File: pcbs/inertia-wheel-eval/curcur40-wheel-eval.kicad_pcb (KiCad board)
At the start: 2 copper layers, 48 x 32 mm, 13 parts, among them J1 SM06B-SRSS-TB, J2 AS5600_Wires, SW1 Kailh_Silent_6.2x6.2, U1 Waveshare_RP2040-Zero

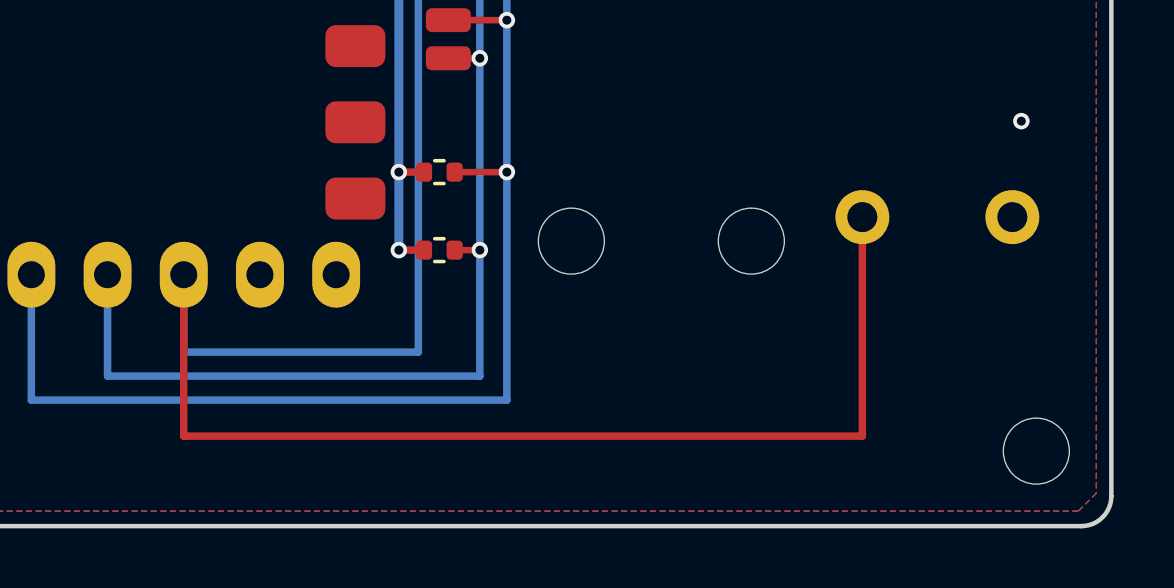
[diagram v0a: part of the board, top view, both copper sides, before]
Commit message: feat(pcb): trim wheel-sensor upper outline for pyramid cover and align eval SW1
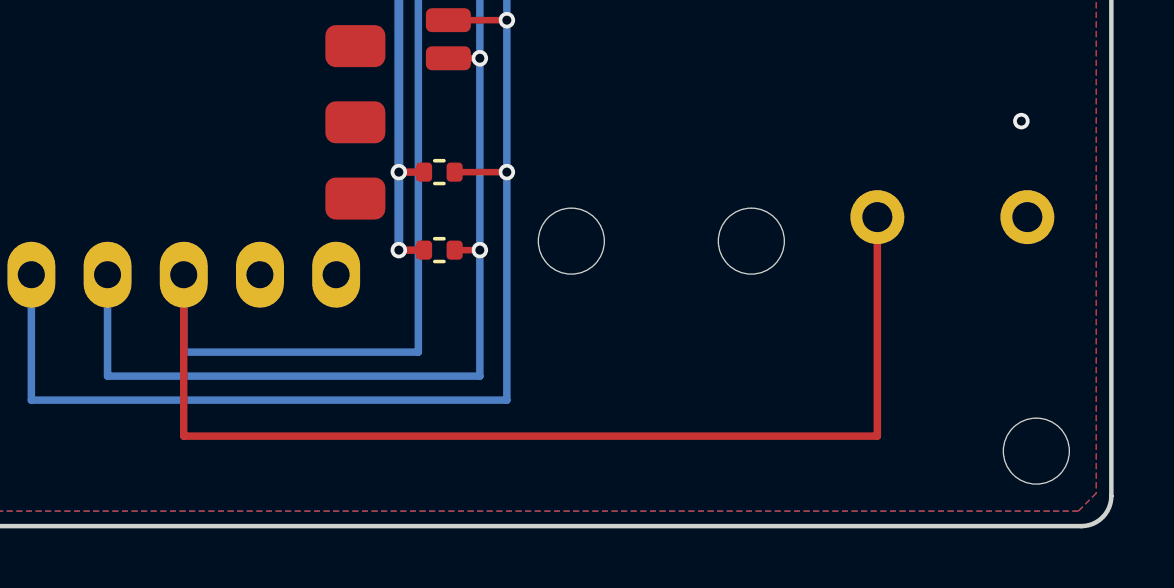
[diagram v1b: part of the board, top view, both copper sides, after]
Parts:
- moved SW1 0.50 mm to (118.7, 105.7)
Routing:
- net /SW_MID: track 68.1 -> 68.6 mm
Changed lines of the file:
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@@
 				(font
 					(size 1.27 1.27)
+					(thickness 0.15)
 				)
 			)
@@
 				(font
 					(size 1.27 1.27)
+					(thickness 0.15)
 				)
 			)
@@
 	(footprint "kbd:Kailh_Square_Silent_6.2x6.2mm"
 		(layer "F.Cu")
-		(at 118.2 105.7)
+		(at 118.7 105.7)
 		(descr "Kailh Square Silent Micro Switch 6.2x6.2x4.3mm (CMI624301D09)")
 		(property "Reference" "SW1"
@@
 				(font
 					(size 1.27 1.27)
+					(thickness 0.15)
 				)
 			)
@@
 				(font
 					(size 1.27 1.27)
+					(thickness 0.15)
 				)
 			)
@@
 	)
 	(segment
+		(start 103.85 99.135)
+		(end 101.9 99.135)
+		(width 0.22)
+		(layer "F.Cu")
+		(net "/SDA")
+	)
+	(segment
+		(start 103.85 104.2)
+		(end 102.11 104.2)
+		(width 0.22)
+		(layer "F.Cu")
+		(net "/SDA")
+	)
+	(segment
+		(start 104.5 92.2)
+		(end 104.5 89.4)
+		(width 0.22)
+		(layer "F.Cu")
+		(net "/SDA")
+	)
+	(via
+		(at 103.85 104.2)
+		(size 0.55)
+		(drill 0.3)
+		(layers "F.Cu" "B.Cu")
+		(net "/SDA")
+	)
+	(via
+		(at 103.85 99.135)
+		(size 0.55)
+		(drill 0.3)
+		(layers "F.Cu" "B.Cu")
+		(net "/SDA")
+	)
+	(via
+		(at 104.5 92.2)
+		(size 0.55)
+		(drill 0.3)
+		(layers "F.Cu" "B.Cu")
+		(net "/SDA")
+	)
+	(segment
+		(start 103.85 104.2)
+		(end 103.85 99.135)
+		(width 0.25)
+		(layer "B.Cu")
+		(net "/SDA")
+	)
+	(segment
+		(start 88 107.62)
+		(end 88 111.8)
+		(width 0.25)
+		(layer "B.Cu")
+		(net "/SDA")
+	)
+	(segment
+		(start 88 111.8)
+		(end 103.85 111.8)
+		(width 0.25)
+		(layer "B.Cu")
+		(net "/SDA")
+	)
+	(segment
+		(start 103.85 111.8)
+		(end 103.85 104.2)
+		(width 0.25)
+		(layer "B.Cu")
+		(net "/SDA")
+	)
+	(segment
+		(start 103.85 99.135)
+		(end 103.85 92.2)
+		(width 0.25)
+		(layer "B.Cu")
+		(net "/SDA")
+	)
+	(segment
+		(start 103.85 92.2)
+		(end 104.5 92.2)
+		(width 0.25)
+		(layer "B.Cu")
+		(net "/SDA")
+	)
+	(segment
 		(start 103.5 91.4)
 		(end 103.5 89.4)
@@
 	)
 	(segment
-		(start 103.85 99.135)
-		(end 101.9 99.135)
-		(width 0.22)
-		(layer "F.Cu")
-		(net "/SDA")
-	)
-	(segment
-		(start 103.85 104.2)
-		(end 102.11 104.2)
-		(width 0.22)
-		(layer "F.Cu")
-		(net "/SDA")
-	)
-	(segment
-		(start 104.5 92.2)
-		(end 104.5 89.4)
-		(width 0.22)
-		(layer "F.Cu")
-		(net "/SDA")
-	)
-	(via
-		(at 103.85 104.2)
-		(size 0.55)
-		(drill 0.3)
-		(layers "F.Cu" "B.Cu")
-		(net "/SDA")
-	)
-	(via
-		(at 103.85 99.135)
-		(size 0.55)
-		(drill 0.3)
-		(layers "F.Cu" "B.Cu")
-		(net "/SDA")
-	)
-	(via
-		(at 104.5 92.2)
-		(size 0.55)
-		(drill 0.3)
-		(layers "F.Cu" "B.Cu")
-		(net "/SDA")
-	)
-	(segment
-		(start 103.85 104.2)
-		(end 103.85 99.135)
-		(width 0.25)
-		(layer "B.Cu")
-		(net "/SDA")
-	)
-	(segment
-		(start 88 107.62)
-		(end 88 111.8)
-		(width 0.25)
-		(layer "B.Cu")
-		(net "/SDA")
-	)
-	(segment
-		(start 88 111.8)
-		(end 103.85 111.8)
-		(width 0.25)
-		(layer "B.Cu")
-		(net "/SDA")
-	)
-	(segment
-		(start 103.85 111.8)
-		(end 103.85 104.2)
-		(width 0.25)
-		(layer "B.Cu")
-		(net "/SDA")
-	)
-	(segment
-		(start 103.85 99.135)
-		(end 103.85 92.2)
-		(width 0.25)
-		(layer "B.Cu")
-		(net "/SDA")
-	)
-	(segment
-		(start 103.85 92.2)
-		(end 104.5 92.2)
-		(width 0.25)
-		(layer "B.Cu")
-		(net "/SDA")
-	)
-	(segment
 		(start 102.5 90.6)
 		(end 102.5 89.4)
@@
 	)
 	(segment
-		(start 115.7 113)
-		(end 115.7 105.7)
+		(start 116.2 113)
+		(end 116.2 105.7)
 		(width 0.25)
 		(layer "F.Cu")
@@
 	(segment
 		(start 93.08 113)
-		(end 115.7 113)
+		(end 116.2 113)
 		(width 0.25)
 		(layer "F.Cu")

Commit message: feat(pcb): integrate sunk inertia wheel cutout and rJ5 connector into curcur40-right and top plate
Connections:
- J1 pad 6: unconnected-(J1-Pin_6-Pad6) -> GND
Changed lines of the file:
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@@
 			(layers "F.Cu" "F.Mask" "F.Paste")
 			(roundrect_rratio 0.25)
-			(net "unconnected-(J1-Pin_6-Pad6)")
+			(net "GND")
 		)
 		(pad "MP" smd roundrect
